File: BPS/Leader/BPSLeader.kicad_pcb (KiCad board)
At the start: 2 copper layers, 100 x 75 mm, 154 parts, among them J1 GPIO Analyzer, J10 CAN_Out, J11 ErrorLightConn, J12 USB_B_Micro, J13 FanBrdConn, J2 Volt/Temp SPI Analyzer, J3 Current SPI Analyzer, J4 CAN Analyzer, J5 SWD, J6 PowerConn, J7 MinionConn, J8 CurrentConn, J9 ContactorConn, Q1 NTR4003NT1G, Q2 VND5N07-E, Q3 NTR4003NT1G, Q4 VND5N07-E, SW1 B3SL-1002P, U1 STM32F413RHTx, U10 ADM3055E, U11 CDSOT23-T24CAN, U12 SI8261ABC-IS, U13 CP2102N-A01-GQFN24, U14 SI8261ABC-IS, U15 SI8261ABC-IS, U16 SI8261ABC-IS, U17 SI8261ABC-IS, U18 MCP112, U19 RN4871, U2 RI3-1205S, U3 NCP1117-3.3_SOT223, U4 M24128, U5 LTC6820, U6 LTC6820, U7 HX1188FNL, U8 SI8261ABC-IS, U9 BAS70-04, Y1 8M

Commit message: Everything traced in leader board except for power circuitry
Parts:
- moved C14 41.0 mm to (146.5, 143.8), turned to 270 degrees
- moved U2 38.4 mm to (142.0, 142.5), turned to 270 degrees
- moved TP1 35.3 mm to (113.0, 140.0)
- moved TP2 35.3 mm to (105.0, 140.0)
- moved L1 34.9 mm to (134.0, 140.0)
- moved TP6 4.61 mm to (156.5, 74.5)
- moved C16 1.25 mm to (140.2, 84.0)
- moved R2 1.25 mm to (145.8, 85.5)
- moved R3 1.25 mm to (145.8, 89.5)
- moved U4 1.25 mm to (140.2, 86.0)
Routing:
- net +5V: track 76.6 -> 222.3 mm, vias 7 -> 15
- net +3V3: track 123.3 -> 252.2 mm, vias 11 -> 16
- net /CAN1_RX: track 7.59 -> 95.2 mm, vias 0 -> 4
- net /CAN1_TX: track 6.84 -> 86.5 mm, vias 0 -> 4
- net Net-(Q3-Pad3): track 0.00 -> 68.7 mm, vias 0 -> 4
- net GND: track 117.5 -> 179.9 mm, vias 14 -> 23
- net +12V: track 3.73 -> 45.3 mm, vias 0 -> 6
- net /PB1: track 6.89 -> 41.1 mm, vias 1 -> 4
- net GNDPWR: track 0.00 -> 33.9 mm, vias 0 -> 15
- net /PB0: track 8.34 -> 36.1 mm, vias 1 -> 2
- net /PA9: track 9.45 -> 30.0 mm, vias 1 -> 2
- net Net-(R33-Pad2): track 0.00 -> 20.5 mm, vias 0 -> 1
- net Net-(D11-Pad1): track 0.00 -> 19.5 mm
- net /Fan Board Interface/FAN2: track 0.00 -> 17.8 mm
- net /I2C3_SCL: track 7.59 -> 23.8 mm, vias 1 -> 2
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- added copper zone on B.Cu, net GND

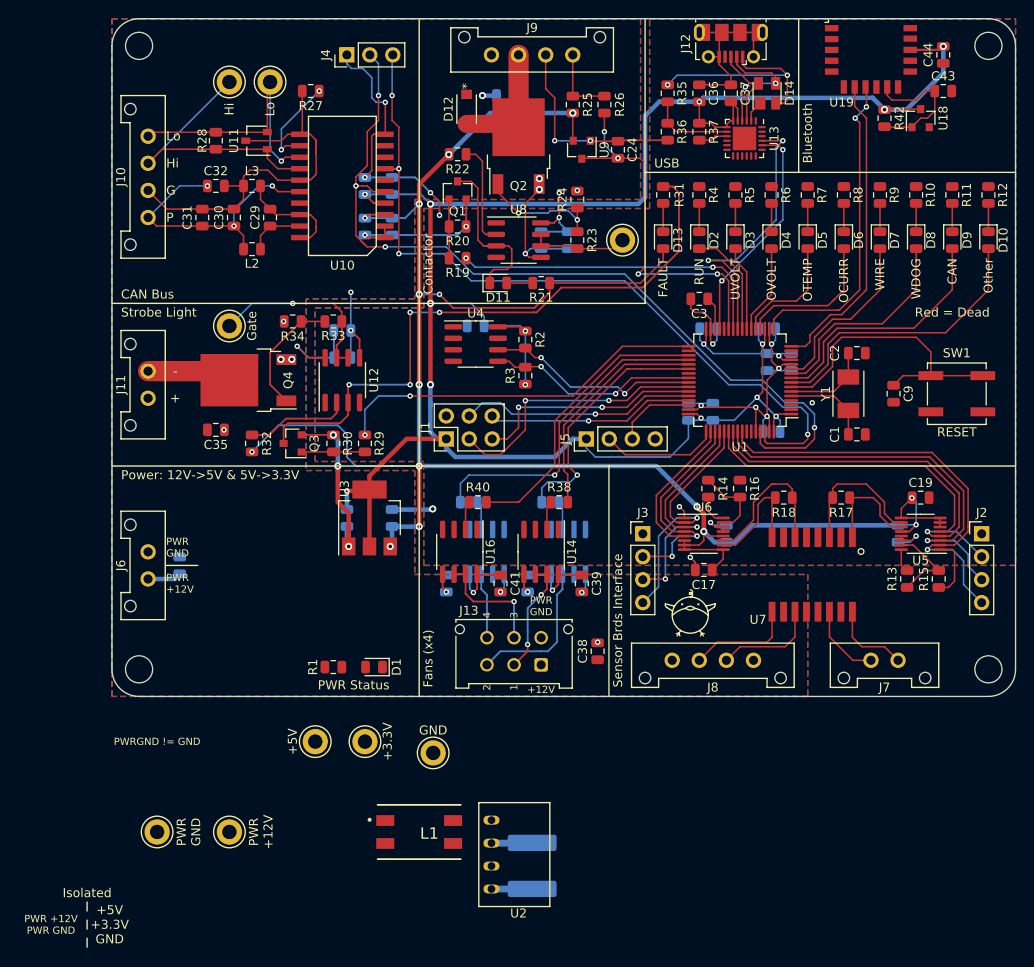
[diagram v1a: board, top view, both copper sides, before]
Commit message: Traces power components
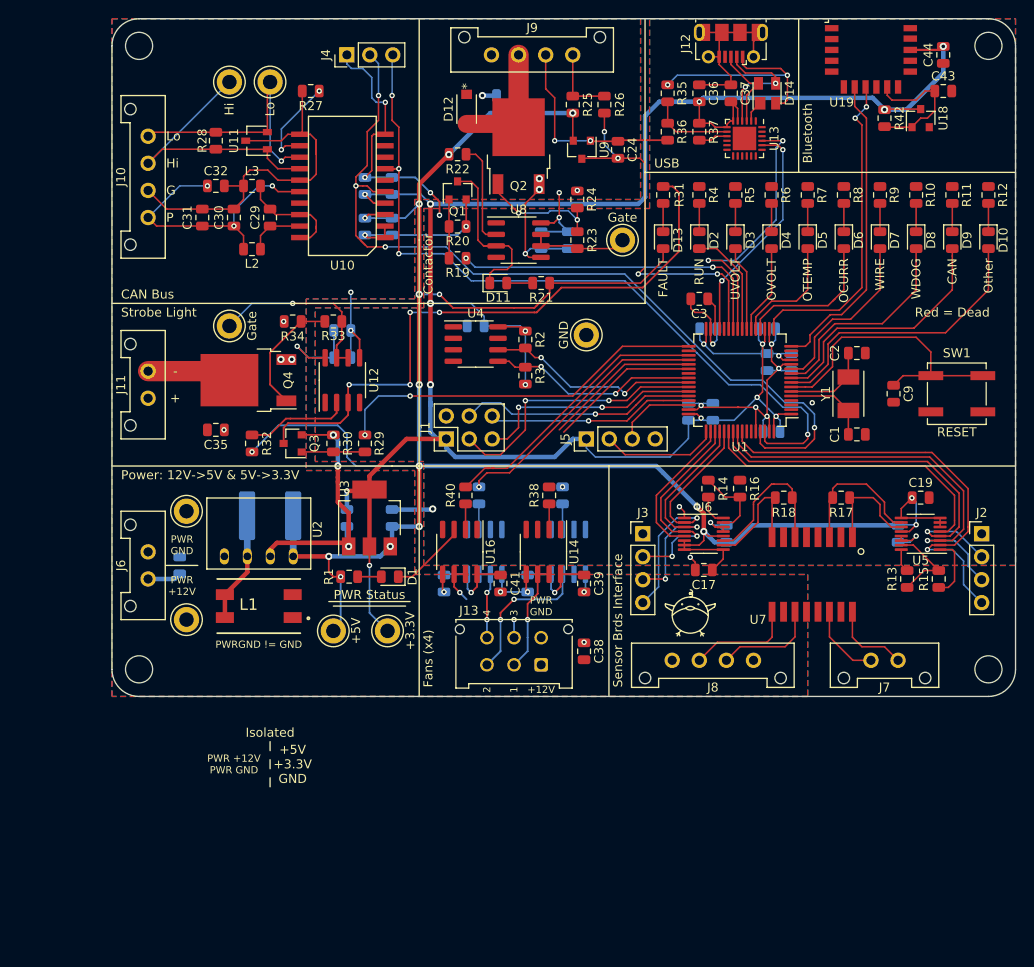
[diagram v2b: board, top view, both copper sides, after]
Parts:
- moved TP5 49.3 mm to (152.5, 85.0), turned to 90 degrees
- moved C14 48.4 mm to (117.5, 105.0), turned to 0 degrees
- moved U2 41.9 mm to (116.2, 109.5), turned to 0 degrees
- moved TP2 35.6 mm to (108.2, 104.5), turned to 270 degrees
- moved L1 30.7 mm to (116.2, 115.0), turned to 180 degrees
- moved TP1 24.0 mm to (108.2, 116.5)
- moved TP3 12.5 mm to (130.5, 117.8)
- moved TP4 12.4 mm to (124.5, 117.8)
- moved D1 10.2 mm to (130.8, 111.8)
- moved R1 10.2 mm to (126.2, 111.8)
- moved R39 1.56 mm to (149.9, 102.8), turned to 90 degrees
- moved R40 1.56 mm to (139.1, 102.8), turned to 90 degrees
- moved C38 1.50 mm to (152.2, 120.0)
- moved R38 1.34 mm to (148.4, 102.8), turned to 90 degrees
- moved R41 1.34 mm to (140.6, 102.8), turned to 90 degrees
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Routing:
- net +5V: track 222.3 -> 243.1 mm, vias 15 -> 17
- net GND: track 179.9 -> 198.5 mm
- net /TIM3_CH2: track 27.8 -> 16.7 mm
- net +3V3: track 252.2 -> 262.4 mm, vias 16 -> 17
- net /TIM3_CH1: track 25.3 -> 17.3 mm
- net Net-(C14-Pad1): track 4.51 -> 12.3 mm
- net /TIM12_CH2: track 36.1 -> 29.4 mm
- net /Fan Board Interface/FAN3: track 13.2 -> 6.62 mm, vias 1 -> 2
- net Net-(D1-Pad2): track 0.00 -> 2.62 mm
- net GNDPWR: track 33.9 -> 36.4 mm
- net +12V: track 45.3 -> 46.1 mm
- net /TIM12_CH1: track 32.0 -> 31.2 mm
- net /Fan Board Interface/FAN1: track 12.8 -> 12.4 mm, vias 2 -> 1
- net /Fan Board Interface/FAN2: track 17.8 -> 17.5 mm, vias 0 -> 2
- net /Fan Board Interface/FAN4: track 8.56 -> 8.45 mm, vias 0 -> 2

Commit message: Finished leader board
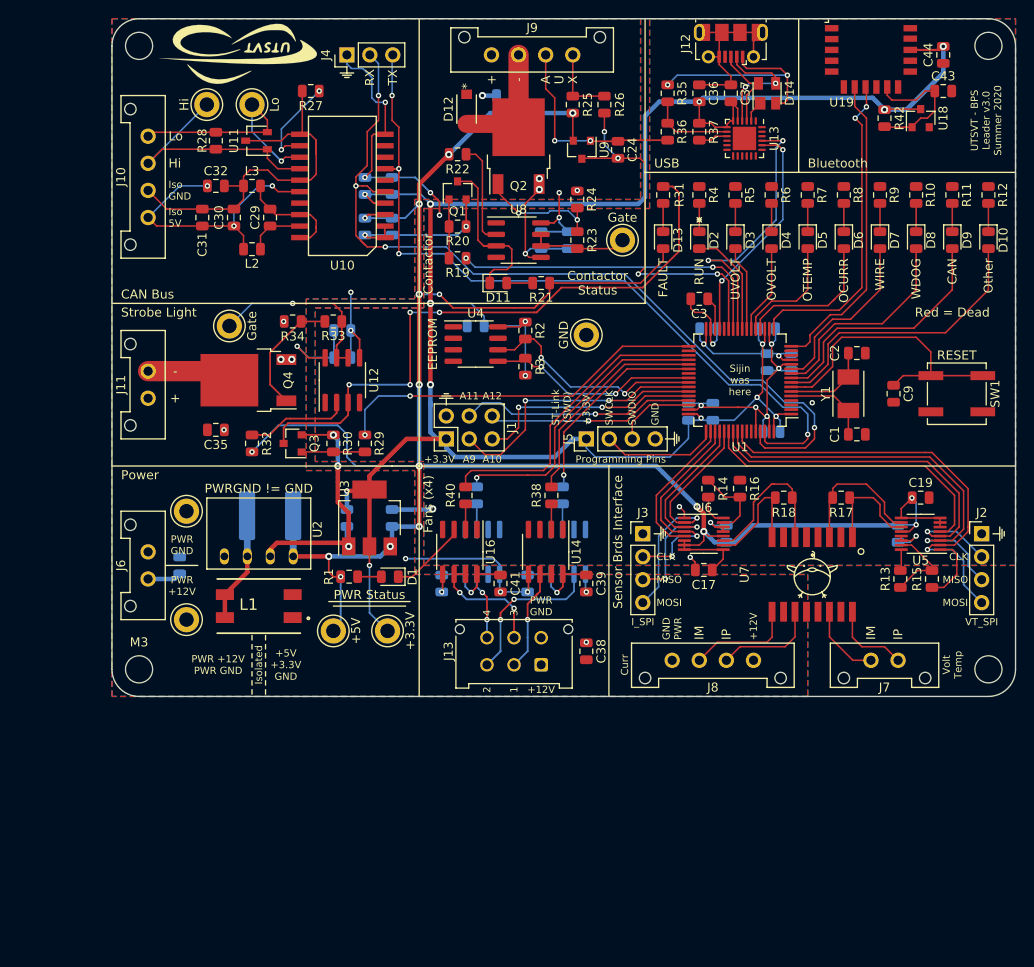
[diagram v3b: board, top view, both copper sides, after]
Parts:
- added LOGO2: Dr. Hallock, UTSVT_Special:Hallock_Image_Small, B.Cu at (184.5, 77.0)
- added LOGO3: UTSVT Logo, UTSVT_Special:UTSVT_Logo_Symbol, F.Cu at (114.2, 53.8)
- moved TP7 3.54 mm to (110.5, 59.5), turned to 270 degrees
- moved TP8 3.20 mm to (115.5, 59.5), turned to 90 degrees
- moved R2 1.00 mm to (145.8, 84.5)
- moved R3 1.00 mm to (145.8, 88.5)
- moved R13 0.75 mm to (187.2, 112.0)
- moved R15 0.75 mm to (190.8, 112.0)
- moved C38 0.25 mm to (152.5, 120.0)
- moved C39 0.25 mm to (152.5, 112.5)
- moved C42 0.25 mm to (136.5, 112.5)
- moved R38 0.25 mm to (148.6, 102.8)
- moved R41 0.25 mm to (140.4, 102.8)
- moved U14 0.25 mm to (148.0, 109.0)
- moved U17 0.25 mm to (141.0, 109.0)
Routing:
- net GNDPWR: track 36.4 -> 48.0 mm, vias 15 -> 16
- net /Fan Board Interface/FAN3: track 6.62 -> 13.5 mm
- net /TIM3_CH1: track 17.3 -> 24.0 mm
- net /TIM3_CH2: track 16.7 -> 22.8 mm
- net /CAN/CAN_H: track 31.7 -> 28.1 mm
- net /TIM12_CH2: track 29.4 -> 32.4 mm
- net /TIM12_CH1: track 31.2 -> 34.0 mm
- net /CAN/CAN_L: track 30.5 -> 28.7 mm
- net /I2C3_SCL: track 23.8 -> 25.4 mm
- net /Fan Board Interface/FAN2: track 17.5 -> 18.7 mm
- net GND: track 198.5 -> 199.2 mm
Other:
- board text added: "A"
- board text added: "A10"
- board text added: "A11"
- board text added: "A12"
- board text added: "A9"
- board text added: "CLK"
- board text added: "Contactor Status"
- board text added: "Curr"
- board text added: "Dr. Gary Hallock"
- board text added: "EEPROM"
- board text added: "GND PWR"
- board text added: "IM"
- board text added: "IP"
- board text added: "I_SPI"
- board text added: "Iso 5V"
- board text added: "Iso GND"
- board text added: "M3"
- board text added: "MISO"
- board text added: "MOSI"
- board text added: "Power"
- board text added: "Programming Pins"
- board text added: "RX"
- board text added: "ST-Link (SWD)"
- board text added: "SWCLK"
- board text added: "SWDIO"
- board text added: "Sijin was here"
- board text added: "TX"
- board text added: "U"
- board text added: "UTSVT - BPS Leader v3.0 Summer 2020"
- board text added: "VT_SPI"
- board text added: "Volt Temp"
- board text added: "X"
- board text removed: "G"
- board text removed: "P"
- board text removed: "Power: 12V->5V & 5V->3.3V"

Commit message: Simplifies dc-dc converter schematics
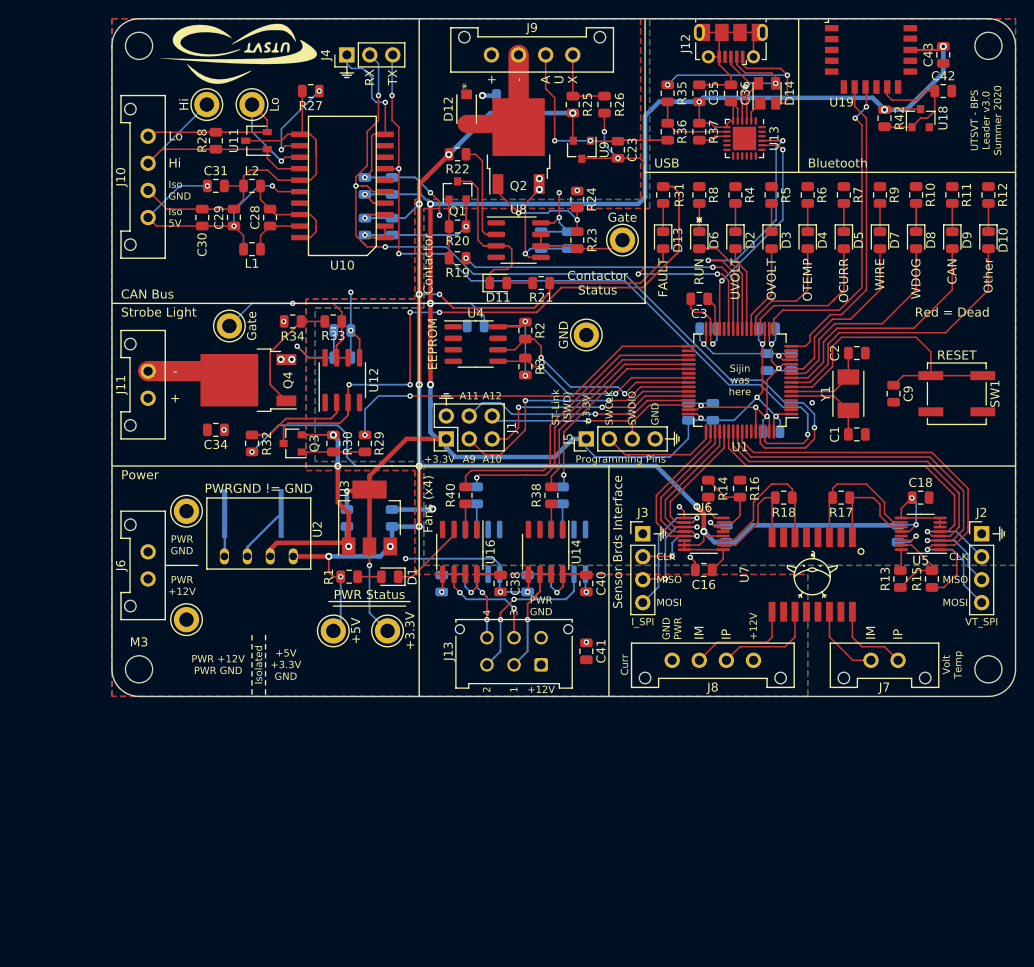
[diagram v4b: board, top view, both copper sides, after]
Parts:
- removed the C14 at (117.5, 105.0)
- removed the L1 at (116.2, 115.0)
- C12: value 4.7u -> 10u; footprint Capacitor_SMD:C_0805_2012Metric -> UTSVT_Passive:C_2220_5750Metric
- U19: value RN4871 -> RN4871-I
- moved C12 9.93 mm to (115.6, 104.8), turned to 180 degrees
- renumbered C15 to C14, C16 to C15, C17 to C16, C18 to C17, C19 to C18, C20 to C19, C22 to C20, C23 to C22, C24 to C23, C25 to C24, C26 to C25, C27 to C26, C28 to C27, C29 to C28, C30 to C29, C31 to C30, C32 to C31, C34 to C32, C35 to C34, C36 to C35, C37 to C36, C40 to C37, C41 to C38, C42 to C39, C39 to C40, C38 to C41, C43 to C42, C44 to C43, D3 to D2, D4 to D3, D5 to D4, D6 to D5, D2 to D6, L2 to L1, L3 to L2, LOGO2 to LOGO1, LOGO3 to LOGO2, R5 to R4, R6 to R5, R7 to R6, R8 to R7, R4 to R8, TP4 to TP3, TP5 to TP4, TP3 to TP5
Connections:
- C16 pad 1: +5V -> +3V3
- J12 pad 4: (no net) -> Net-(J12-Pad4)
- U1 pad 14: (no net) -> Net-(U1-Pad14)
- U1 pad 15: (no net) -> Net-(U1-Pad15)
- U1 pad 2: (no net) -> Net-(U1-Pad2)
- U1 pad 28: (no net) -> Net-(U1-Pad28)
- U1 pad 3: (no net) -> Net-(U1-Pad3)
- U1 pad 34: (no net) -> Net-(U1-Pad34)
- U1 pad 39: (no net) -> Net-(U1-Pad39)
- U1 pad 4: (no net) -> Net-(U1-Pad4)
- U1 pad 58: (no net) -> Net-(U1-Pad58)
- U1 pad 59: (no net) -> Net-(U1-Pad59)
- U10 pad 17: (no net) -> Net-(U10-Pad17)
- U10 pad 6: (no net) -> Net-(U10-Pad6)
- U10 pad 8: (no net) -> Net-(U10-Pad8)
- U10 pad 9: (no net) -> Net-(U10-Pad9)
- U12 pad 1: (no net) -> Net-(U12-Pad1)
- U12 pad 4: (no net) -> Net-(U12-Pad4)
- U13 pad 1: (no net) -> Net-(U13-Pad1)
- U13 pad 10: (no net) -> Net-(U13-Pad10)
- U13 pad 11: (no net) -> Net-(U13-Pad11)
- U13 pad 12: (no net) -> Net-(U13-Pad12)
- U13 pad 13: (no net) -> Net-(U13-Pad13)
- U13 pad 14: (no net) -> Net-(U13-Pad14)
- U13 pad 15: (no net) -> Net-(U13-Pad15)
- U13 pad 16: (no net) -> Net-(U13-Pad16)
- U13 pad 17: (no net) -> Net-(U13-Pad17)
- U13 pad 18: (no net) -> Net-(U13-Pad18)
- U13 pad 19: (no net) -> Net-(U13-Pad19)
- U13 pad 22: (no net) -> Net-(U13-Pad22)
- U13 pad 23: (no net) -> Net-(U13-Pad23)
- U13 pad 24: (no net) -> Net-(U13-Pad24)
- U14 pad 1: (no net) -> Net-(U14-Pad1)
- U14 pad 4: (no net) -> Net-(U14-Pad4)
- U15 pad 1: (no net) -> Net-(U15-Pad1)
- U15 pad 4: (no net) -> Net-(U15-Pad4)
- U16 pad 1: (no net) -> Net-(U16-Pad1)
- U16 pad 4: (no net) -> Net-(U16-Pad4)
- U17 pad 1: (no net) -> Net-(U17-Pad1)
- U17 pad 4: (no net) -> Net-(U17-Pad4)
- U19 pad 1: (no net) -> Net-(U19-Pad1)
- U19 pad 11: (no net) -> Net-(U19-Pad11)
- U19 pad 12: (no net) -> Net-(U19-Pad12)
- U19 pad 15: (no net) -> Net-(U19-Pad15)
- U19 pad 16: (no net) -> Net-(U19-Pad16)
- U19 pad 3: (no net) -> Net-(U19-Pad3)
- U19 pad 4: (no net) -> Net-(U19-Pad4)
- U19 pad 5: (no net) -> Net-(U19-Pad5)
- U19 pad 6: (no net) -> Net-(U19-Pad6)
- U19 pad 9: (no net) -> Net-(U19-Pad9)
- U2 pad 2: Net-(C14-Pad1) -> +12V
- U5 pad 6: +5V -> +3V3
- U5 pad 7: +5V -> +3V3
- U5 pad 8: +5V -> +3V3
- U7 pad 10: (no net) -> Net-(U7-Pad10)
- U7 pad 15: (no net) -> Net-(U7-Pad15)
- U7 pad 2: (no net) -> Net-(U7-Pad2)
- U7 pad 7: (no net) -> Net-(U7-Pad7)
- U8 pad 1: (no net) -> Net-(U8-Pad1)
- U8 pad 4: (no net) -> Net-(U8-Pad4)
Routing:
- net Net-(C14-Pad1): track 12.3 -> 0.00 mm
- net GNDPWR: track 48.0 -> 52.8 mm
- net +5V: track 243.1 -> 238.6 mm
- net +12V: track 46.3 -> 48.9 mm

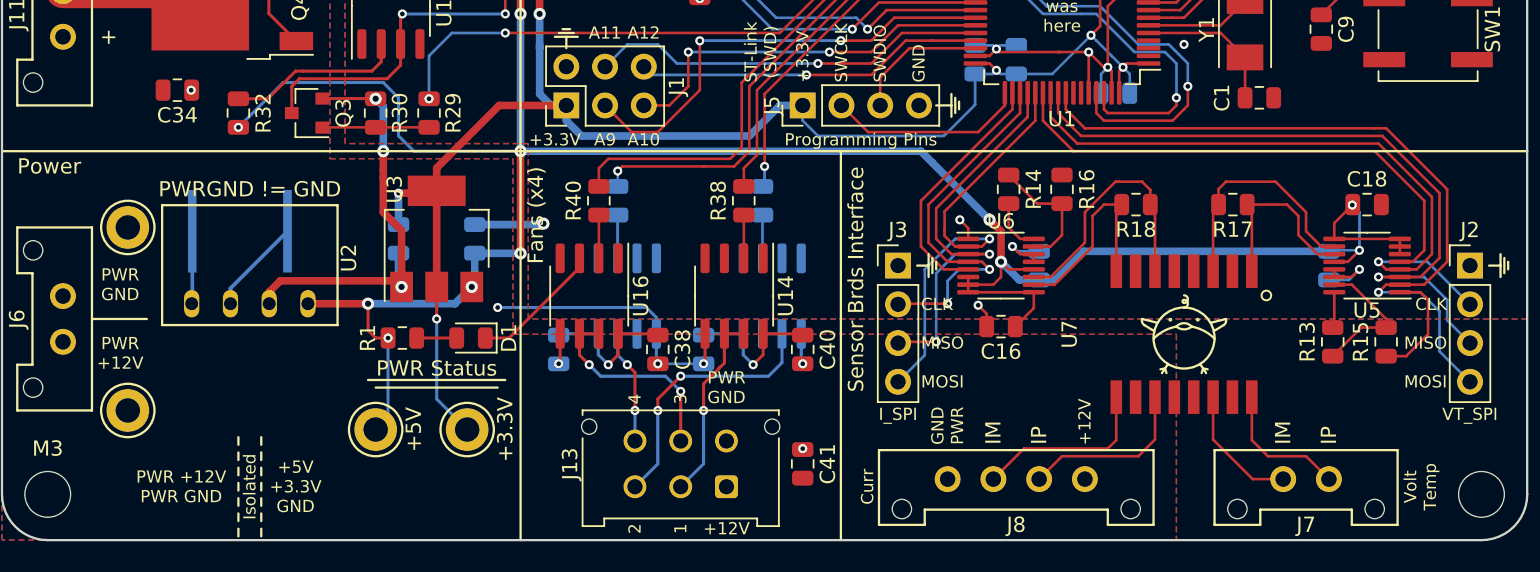
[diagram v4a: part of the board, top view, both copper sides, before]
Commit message: Finishes new power circuitry tracing
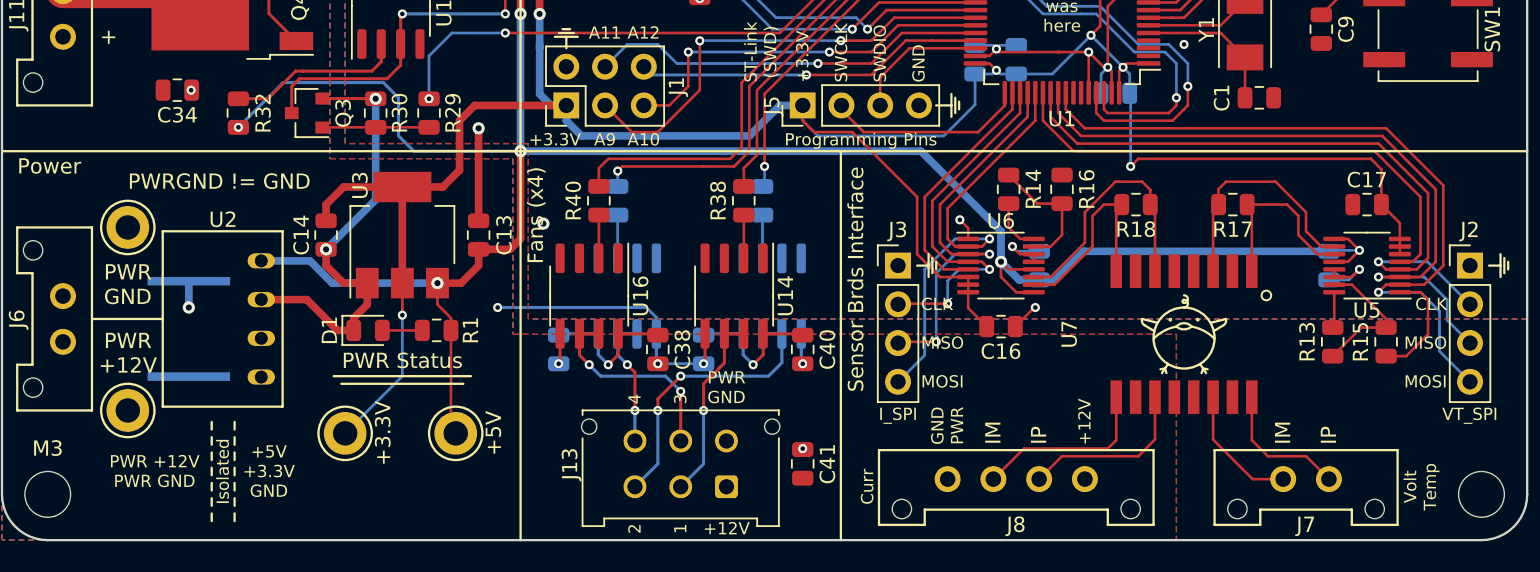
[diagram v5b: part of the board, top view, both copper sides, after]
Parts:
- C13, C14, C17: moved to F.Cu
- C18: moved to B.Cu
- moved C17 21.9 mm to (189.5, 103.0), turned to 180 degrees
- moved C18 21.9 mm to (168.0, 107.0), turned to 90 degrees
- moved TP5 8.00 mm to (122.5, 118.0)
- moved C12 7.22 mm to (112.2, 111.2), turned to 270 degrees
- moved D1 6.77 mm to (124.0, 111.2), turned to 0 degrees
- moved TP3 5.26 mm to (129.8, 118.0)
- moved C14 4.76 mm to (121.2, 105.0)
- moved R1 2.30 mm to (128.5, 111.2), turned to 180 degrees
- moved U3 2.26 mm to (126.2, 105.0)
- moved U2 1.25 mm to (117.0, 110.5), turned to 90 degrees
- moved C13 0.35 mm to (131.2, 105.0)
- turned C16 to 0 degrees
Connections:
- C17 pad 1: +5V -> +3V3
- U6 pad 6: +5V -> +3V3
- U6 pad 7: +5V -> +3V3
- U6 pad 8: +5V -> +3V3
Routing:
- net +3V3: track 262.4 -> 318.5 mm
- net +5V: track 238.6 -> 225.1 mm, vias 17 -> 12
- net GND: track 199.2 -> 192.9 mm
- net GNDPWR: track 52.8 -> 48.0 mm
- net +12V: track 48.9 -> 44.3 mm, vias 6 -> 7

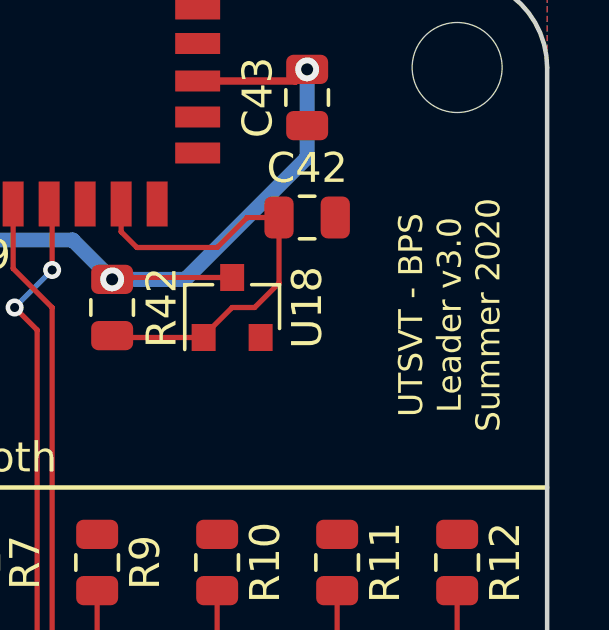
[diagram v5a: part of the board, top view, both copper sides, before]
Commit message: Adds version number to leader_board and creates schematics pdf
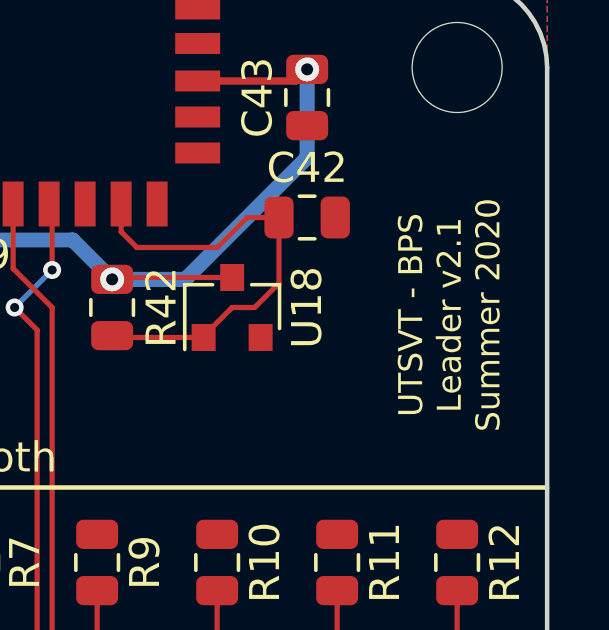
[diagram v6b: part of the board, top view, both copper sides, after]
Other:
- board text added: "UTSVT - BPS Leader v2.1 Summer 2020"
- board text removed: "UTSVT - BPS Leader v3.0 Summer 2020"
